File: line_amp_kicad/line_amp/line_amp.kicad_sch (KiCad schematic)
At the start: 2 parts

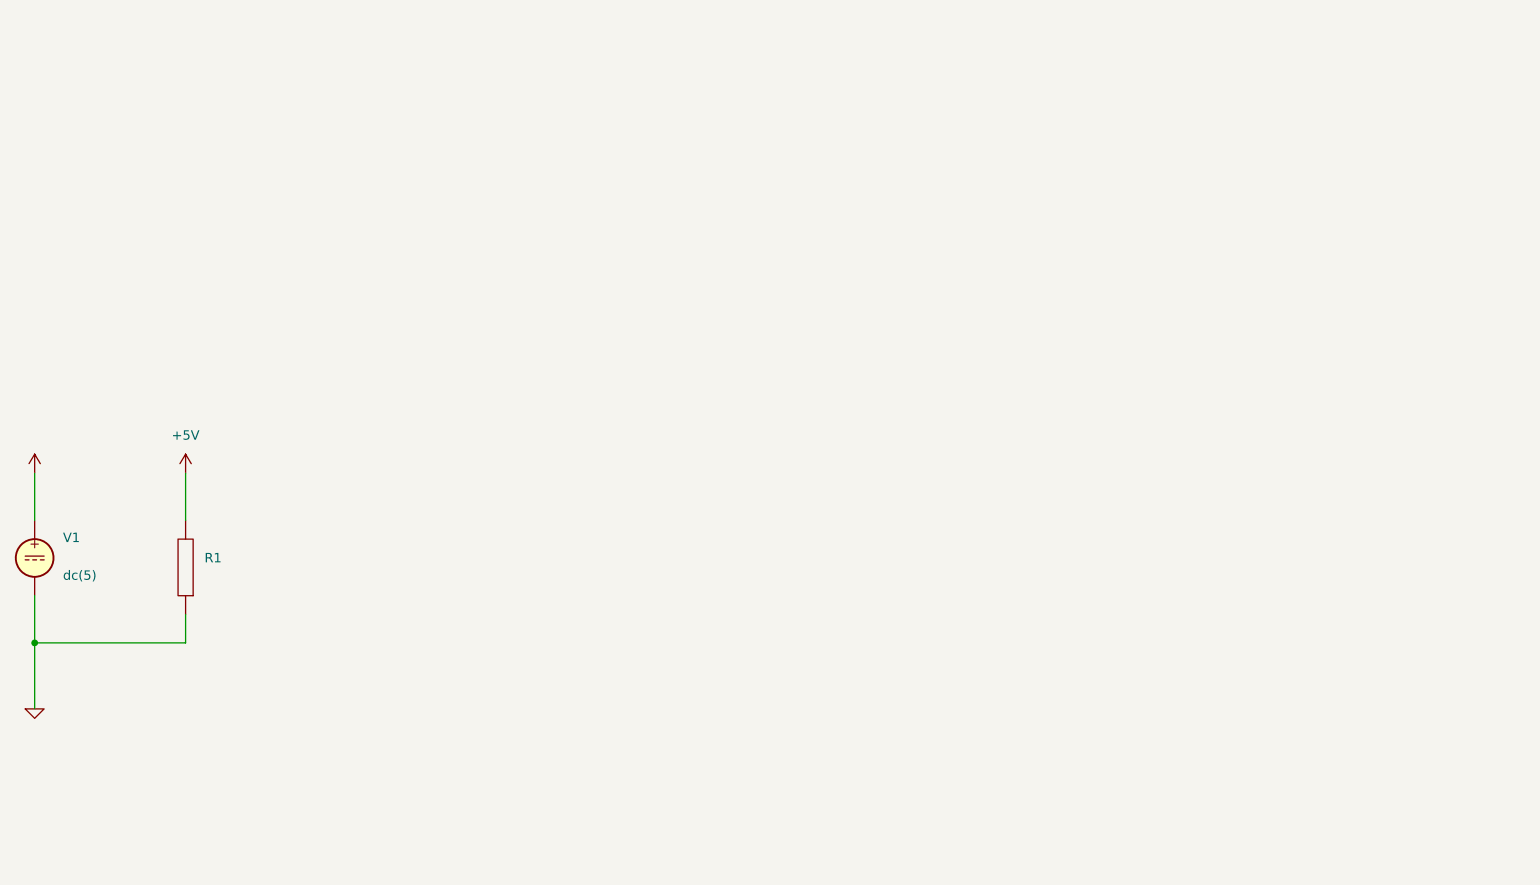
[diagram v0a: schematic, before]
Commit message: spent a lot of time updating sheet template to get title block setup, and get colors right
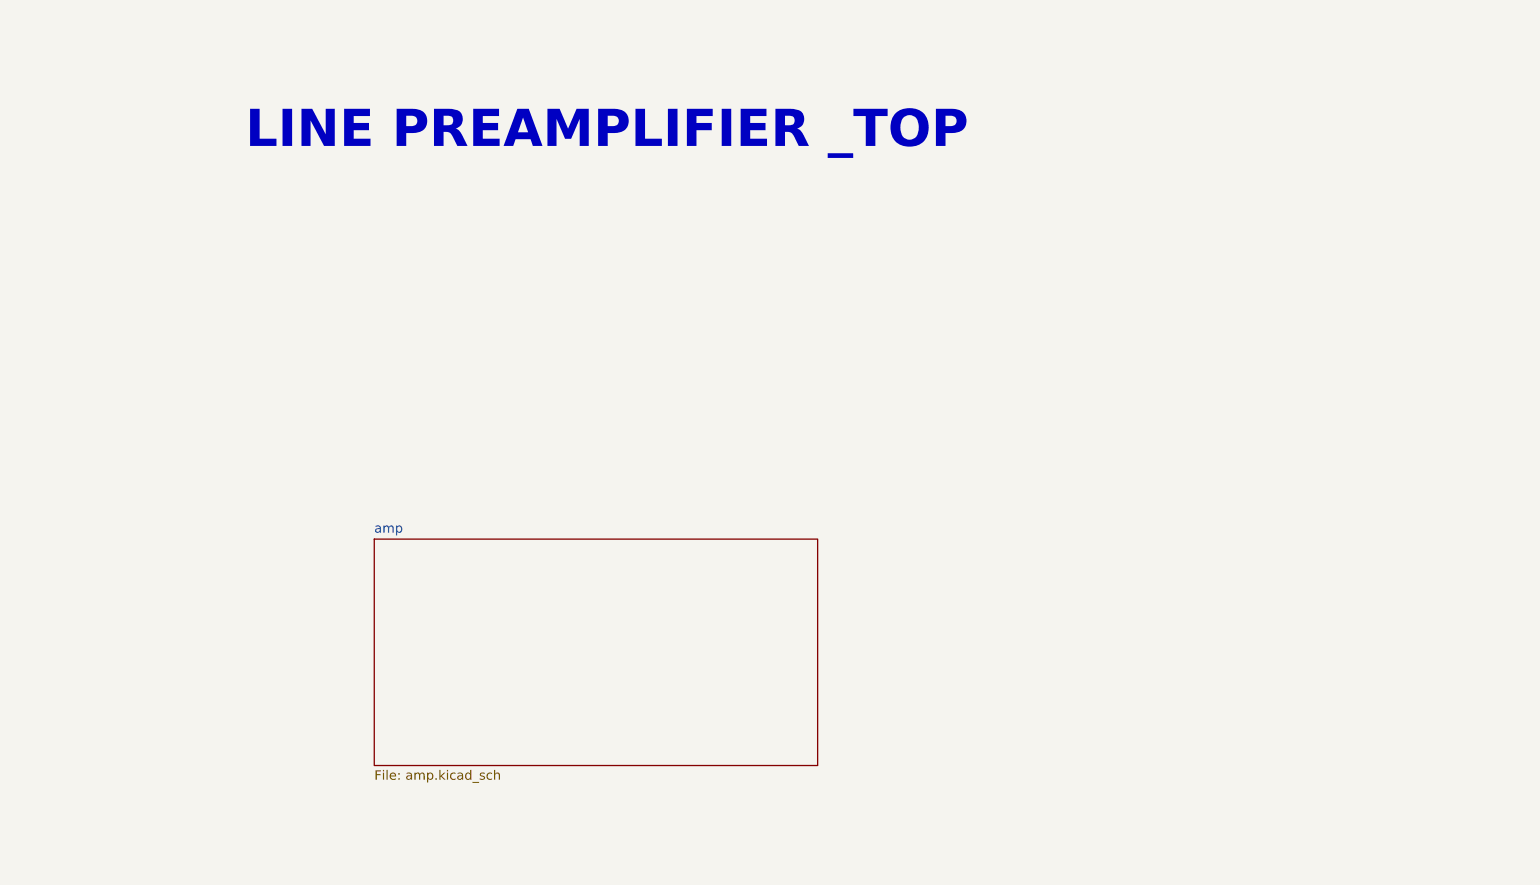
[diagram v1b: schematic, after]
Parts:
- removed R1: (no value), symbol pspice:R
- removed V1: (no value), symbol Simulation_SPICE:VDC
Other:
- added sheet amp (amp.kicad_sch)
- note added: "LINE PREAMPLIFIER _TOP"
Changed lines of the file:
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@@
 (kicad_sch (version 20211123) (generator eeschema)
   (paper "A4")
-  (junction (at 73.66 97.79) (diameter 0) (color 0 0 0 0)
+  (title_block
+    (comment 1 "${PCBA_NAME}")
+    (comment 2 "${PCBA_REV}")
+    (comment 3 "${PCB_ENGINEER}")
+    (comment 4 "${PCBA_PN}")
+    (comment 5 "${PCBA_ID}")
+    (comment 6 "${PCBA_PROJ}")
   )
-  (wire (pts (xy 73.66 74.93) (xy 73.66 81.28))
-    (stroke (width 0) (type default) (color 0 0 0 0))
+  (text "LINE PREAMPLIFIER _TOP\n" (at 199.39 31.75 180)
+    (effects (font (size 5 5) (thickness 1) bold) (justify right bottom))
   )
-  (wire (pts (xy 93.98 74.93) (xy 93.98 81.28))
-    (stroke (width 0) (type default) (color 0 0 0 0))
-  )
-  (wire (pts (xy 73.66 97.79) (xy 73.66 91.44))
-    (stroke (width 0) (type default) (color 0 0 0 0))
-  )
-  (wire (pts (xy 93.98 93.98) (xy 93.98 97.79))
-    (stroke (width 0) (type default) (color 0 0 0 0))
-  )
-  (wire (pts (xy 73.66 97.79) (xy 73.66 106.68))
-    (stroke (width 0) (type default) (color 0 0 0 0))
-  )
-  (wire (pts (xy 93.98 97.79) (xy 73.66 97.79))
-    (stroke (width 0) (type default) (color 0 0 0 0))
-  )
-  (symbol (lib_id "pspice:0") (at 73.66 106.68 0) (unit 1)
-    (in_bom yes) (on_board yes) (fields_autoplaced)
-    (property "Reference" "#GND01" (id 0) (at 73.66 109.22 0)
-      (effects (font (size 1.27 1.27)) hide)
+  (sheet (at 119.38 83.82) (size 59.69 30.48) (fields_autoplaced)
+    (stroke (width 0.1524) (type solid) (color 0 0 0 0))
+    (fill (color 0 0 0 0.0000))
+    (property "Sheet name" "amp" (id 0) (at 119.38 83.1084 0)
+      (effects (font (size 1.27 1.27)) (justify left bottom))
     )
-    (property "Value" "" (id 1) (at 73.66 104.14 0))
-    (property "Footprint" "" (id 2) (at 73.66 106.68 0)
-      (effects (font (size 1.27 1.27)) hide)
+    (property "Sheet file" "amp.kicad_sch" (id 1) (at 119.38 114.8846 0)
+      (effects (font (size 1.27 1.27)) (justify left top))
     )
-    (property "Datasheet" "~" (id 3) (at 73.66 106.68 0)
-      (effects (font (size 1.27 1.27)) hide)
-    )
-    (pin "1")
-  )
-  (symbol (lib_id "pspice:R") (at 93.98 87.63 180) (unit 1)
-    (in_bom yes) (on_board yes) (fields_autoplaced)
-    (property "Reference" "R1" (id 0) (at 96.52 86.3599 0)
-      (effects (font (size 1.27 1.27)) (justify right))
-    )
-    (property "Value" "" (id 1) (at 96.52 88.8999 0)
-      (effects (font (size 1.27 1.27)) (justify right))
-    )
-    (property "Footprint" "" (id 2) (at 93.98 87.63 0)
-      (effects (font (size 1.27 1.27)) hide)
-    )
-    (property "Datasheet" "~" (id 3) (at 93.98 87.63 0)
-      (effects (font (size 1.27 1.27)) hide)
-    )
-    (pin "1")
-    (pin "2")
-  )
-  (symbol (lib_id "power:+5V") (at 93.98 74.93 0) (unit 1)
-    (in_bom yes) (on_board yes) (fields_autoplaced)
-    (property "Reference" "#PWR02" (id 0) (at 93.98 78.74 0)
-      (effects (font (size 1.27 1.27)) hide)
-    )
-    (property "Value" "+5V" (id 1) (at 93.98 69.85 0))
-    (property "Footprint" "" (id 2) (at 93.98 74.93 0)
-      (effects (font (size 1.27 1.27)) hide)
-    )
-    (property "Datasheet" "" (id 3) (at 93.98 74.93 0)
-      (effects (font (size 1.27 1.27)) hide)
-    )
-    (pin "1")
-  )
-  (symbol (lib_id "Simulation_SPICE:VDC") (at 73.66 86.36 0) (unit 1)
-    (in_bom yes) (on_board yes) (fields_autoplaced)
-    (property "Reference" "V1" (id 0) (at 77.47 83.6301 0)
-      (effects (font (size 1.27 1.27)) (justify left))
-    )
-    (property "Value" "" (id 1) (at 77.47 86.1701 0)
-      (effects (font (size 1.27 1.27)) (justify left))
-    )
-    (property "Footprint" "" (id 2) (at 73.66 86.36 0)
-      (effects (font (size 1.27 1.27)) hide)
-    )
-    (property "Datasheet" "~" (id 3) (at 73.66 86.36 0)
-      (effects (font (size 1.27 1.27)) hide)
-    )
-    (property "Spice_Netlist_Enabled" "Y" (id 4) (at 73.66 86.36 0)
-      (effects (font (size 1.27 1.27)) (justify left) hide)
-    )
-    (property "Spice_Primitive" "V" (id 5) (at 73.66 86.36 0)
-      (effects (font (size 1.27 1.27)) (justify left) hide)
-    )
-    (property "Spice_Model" "dc(5)" (id 6) (at 77.47 88.7101 0)
-      (effects (font (size 1.27 1.27)) (justify left))
-    )
-    (pin "1")
-    (pin "2")
-  )
-  (symbol (lib_id "power:+5V") (at 73.66 74.93 0) (unit 1)
-    (in_bom yes) (on_board yes) (fields_autoplaced)
-    (property "Reference" "#PWR01" (id 0) (at 73.66 78.74 0)
-      (effects (font (size 1.27 1.27)) hide)
-    )
-    (property "Value" "" (id 1) (at 73.66 69.85 0))
-    (property "Footprint" "" (id 2) (at 73.66 74.93 0)
-      (effects (font (size 1.27 1.27)) hide)
-    )
-    (property "Datasheet" "" (id 3) (at 73.66 74.93 0)
-      (effects (font (size 1.27 1.27)) hide)
-    )
-    (pin "1")
   )
   (sheet_instances
     (path "/" (page "1"))
-  )
-  (symbol_instances
-    (path "/07fc3d16-b3f7-45de-94e3-03ae3ae0303a"
-      (reference "#GND01") (unit 1) (value "0") (footprint "")
-    )
-    (path "/ee56e7fd-0b29-4af5-bc9c-d62d1d9ed30f"
-      (reference "#PWR01") (unit 1) (value "+5V") (footprint "")
-    )
-    (path "/6fc82615-27b5-4883-b630-e7178cb33280"
-      (reference "#PWR02") (unit 1) (value "+5V") (footprint "")
-    )
-    (path "/6289737d-0f99-4c8f-8987-9417edb7a6de"
-      (reference "R1") (unit 1) (value "470") (footprint "")
-    )
-    (path "/945e3679-e028-495e-a37f-21f134c76f63"
-      (reference "V1") (unit 1) (value "VDC") (footprint "")
-    )
+    (path "/86c9a117-d4e0-4b94-b683-c667aba115d1" (page "2"))
   )
 )

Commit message: updates to schematics
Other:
- sheet amp renamed AMP
- added sheet REGULATORS (regulators.kicad_sch)
- note added: "${SHEETNAME}"
- note added: "_TOP"
- note removed: "LINE PREAMPLIFIER _TOP"
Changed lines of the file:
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@@
     (comment 6 "${PCBA_PROJ}")
   )
-  (text "LINE PREAMPLIFIER _TOP\n" (at 199.39 31.75 180)
+  (text "_TOP\n" (at 274.32 26.67 180)
     (effects (font (size 5 5) (thickness 1) bold) (justify right bottom))
   )
-  (sheet (at 119.38 83.82) (size 59.69 30.48) (fields_autoplaced)
+  (text "${SHEETNAME}\n" (at 245.11 21.59 180)
+    (effects (font (size 5 5) (thickness 1) bold) (justify right bottom))
+  )
+  (text "${SHEETNAME}\n" (at 254 21.59 180)
+    (effects (font (size 5 5) (thickness 1) bold) (justify right bottom))
+  )
+  (text "${SHEETNAME}" (at 199.39 31.75 180)
+    (effects (font (size 5 5) (thickness 1) bold) (justify right bottom))
+  )
+  (text "${SHEETNAME}\n" (at 256.54 24.13 180)
+    (effects (font (size 5 5) (thickness 1) bold) (justify right bottom))
+  )
+  (sheet (at 127 63.5) (size 30.48 22.86) (fields_autoplaced)
     (stroke (width 0.1524) (type solid) (color 0 0 0 0))
     (fill (color 0 0 0 0.0000))
-    (property "Sheet name" "amp" (id 0) (at 119.38 83.1084 0)
+    (property "Sheet name" "REGULATORS" (id 0) (at 127 62.7884 0)
       (effects (font (size 1.27 1.27)) (justify left bottom))
     )
-    (property "Sheet file" "amp.kicad_sch" (id 1) (at 119.38 114.8846 0)
+    (property "Sheet file" "regulators.kicad_sch" (id 1) (at 127 86.9446 0)
+      (effects (font (size 1.27 1.27)) (justify left top))
+    )
+  )
+  (sheet (at 127 101.6) (size 30.48 24.13) (fields_autoplaced)
+    (stroke (width 0.1524) (type solid) (color 0 0 0 0))
+    (fill (color 0 0 0 0.0000))
+    (property "Sheet name" "AMP" (id 0) (at 127 100.8884 0)
+      (effects (font (size 1.27 1.27)) (justify left bottom))
+    )
+    (property "Sheet file" "amp.kicad_sch" (id 1) (at 127 126.3146 0)
       (effects (font (size 1.27 1.27)) (justify left top))
     )
@@
     (path "/" (page "1"))
     (path "/86c9a117-d4e0-4b94-b683-c667aba115d1" (page "2"))
+    (path "/25f0dc4a-715b-4730-aa67-011162ff0e7d" (page "3"))
+  )
+  (symbol_instances
+    (path "/86c9a117-d4e0-4b94-b683-c667aba115d1/236282df-5239-4053-8372-dfc1e6f9323e"
+      (reference "#PWR?") (unit 1) (value "GND") (footprint "")
+    )
+    (path "/86c9a117-d4e0-4b94-b683-c667aba115d1/9485359b-1ec0-4221-bb01-0106d929b9f5"
+      (reference "R?") (unit 1) (value "1k") (footprint "")
+    )
+    (path "/86c9a117-d4e0-4b94-b683-c667aba115d1/ce25f997-29d0-47f3-a82a-57acc64259d8"
+      (reference "R?") (unit 1) (value "330") (footprint "")
+    )
+    (path "/86c9a117-d4e0-4b94-b683-c667aba115d1/571dd08f-0ed8-4e76-bf91-f5a224ee71ce"
+      (reference "U?") (unit 1) (value "LM4562") (footprint "")
+    )
+    (path "/86c9a117-d4e0-4b94-b683-c667aba115d1/98ba5dd3-97ee-447f-8351-875c0606d759"
+      (reference "U?") (unit 1) (value "LM4562") (footprint "")
+    )
+    (path "/86c9a117-d4e0-4b94-b683-c667aba115d1/456ef4ab-d417-4be2-99a2-df71bc1589a7"
+      (reference "U?") (unit 2) (value "LM4562") (footprint "")
+    )
+    (path "/86c9a117-d4e0-4b94-b683-c667aba115d1/8ba55066-02f2-4e5d-a63f-6f191fc4623d"
+      (reference "U?") (unit 2) (value "LM4562") (footprint "")
+    )
+    (path "/86c9a117-d4e0-4b94-b683-c667aba115d1/3318370f-2f86-41bf-bca4-3acd1719ba46"
+      (reference "U?") (unit 3) (value "LM4562") (footprint "")
+    )
+    (path "/86c9a117-d4e0-4b94-b683-c667aba115d1/3b375248-509e-4399-a63e-ea73287fefea"
+      (reference "U?") (unit 3) (value "LM4562") (footprint "")
+    )
   )
 )
